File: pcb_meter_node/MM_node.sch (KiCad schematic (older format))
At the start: 60 parts, among them J1 CONN_BATT, J10 CONN_BREAKOUT, J2 CONN_REG, J3 CONN_FTDI, J4 ANT, J5 ANT-UFL, J6 ANT-SMA, J7 CONN_LDR, J9 CONN_CT, M1 MOUNT_HOLE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

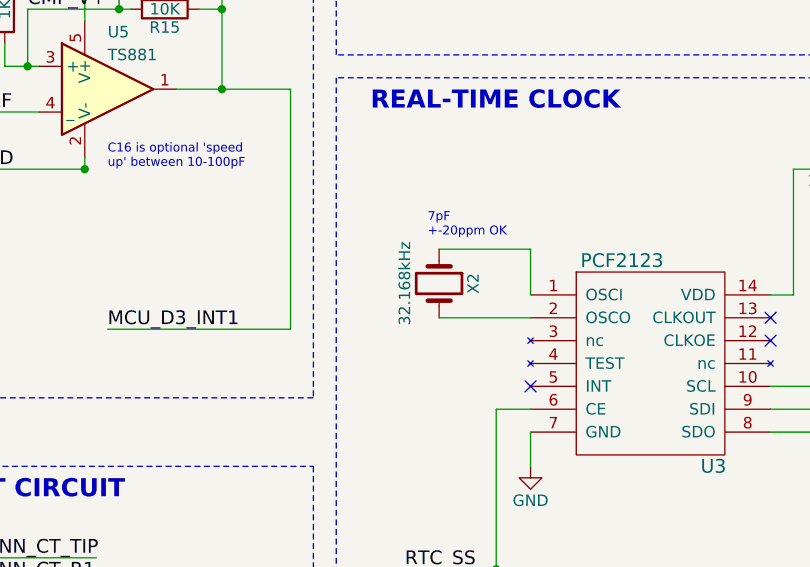
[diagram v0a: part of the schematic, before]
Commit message: R7, minor doc edits
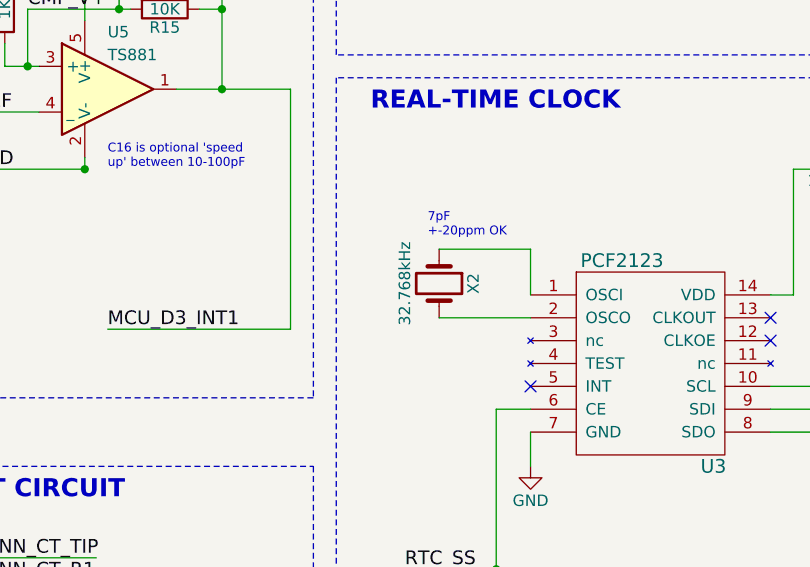
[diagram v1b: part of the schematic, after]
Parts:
- X2: value 32.168kHz -> 32.768kHz
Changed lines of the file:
@@
 P 3300 3400
 F 0 "X2" H 3300 3550 50  0000 C CNN
-F 1 "32.168kHz" H 3300 3250 50  0000 C CNN
+F 1 "32.768kHz" H 3300 3250 50  0000 C CNN
 F 2 "Crystals:Crystal_SMD_EuroQuartz_EQ161-2pin_3.2x1.5mm_HandSoldering" H 3300 3400 50  0001 C CNN
 F 3 "" H 3300 3400 50  0001 C CNN
